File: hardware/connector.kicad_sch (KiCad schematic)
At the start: 5 parts, among them J1 SAFETY_SUPPLY, J2 SWDIO_CONN, J3 SENSORS, J4 VALVES, J5 MAIN

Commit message: DRC fixes part 1
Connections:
- net +24V renamed 24v input
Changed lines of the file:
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@@
-    (stroke (width 0) (type default) (color 0 0 0 0))
-  )
-  (wire (pts (xy 78.74 118.11) (xy 78.74 120.65))
     (stroke (width 0) (type default) (color 0 0 0 0))
   )
@@
     )
   )
+  (global_label "24v input" (shape input) (at 78.74 120.65 180) (fields_autoplaced)
+    (effects (font (size 1.27 1.27)) (justify right))
+    (property "Intersheet References" "${INTERSHEET_REFS}" (id 0) (at 67.195 120.5706 0)
+      (effects (font (size 1.27 1.27)) (justify right) hide)
+    )
+  )
   (global_label "NRST" (shape input) (at 201.93 87.63 180) (fields_autoplaced)
     (effects (font (size 1.27 1.27) italic) (justify right))
@@
       (effects (font (size 1.27 1.27)) hide)
     )
-    (pin "1")
-  )
-  (symbol (lib_id "power:+24V") (at 78.74 118.11 0) (unit 1)
-    (in_bom yes) (on_board yes) (fields_autoplaced)
-    (property "Reference" "#PWR0108" (id 0) (at 78.74 121.92 0)
-      (effects (font (size 1.27 1.27)) hide)
-    )
-    (property "Value" "+24V" (id 1) (at 78.74 113.03 0))
-    (property "Footprint" "" (id 2) (at 78.74 118.11 0)
-      (effects (font (size 1.27 1.27)) hide)
-    )
-    (property "Datasheet" "" (id 3) (at 78.74 118.11 0)
-      (effects (font (size 1.27 1.27)) hide)
-    )

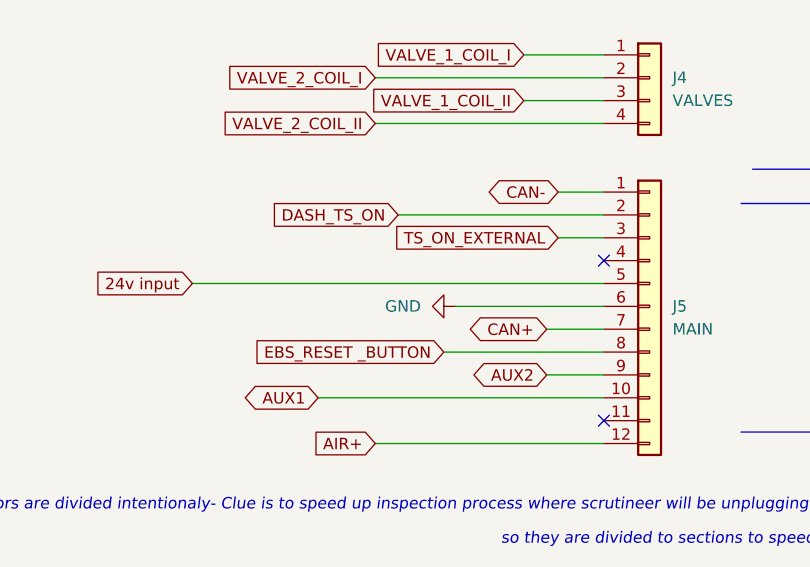
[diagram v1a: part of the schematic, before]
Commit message: Alpha 1.0 Hardware relase. 0xDRC state, improved aesthetics and signal integrity
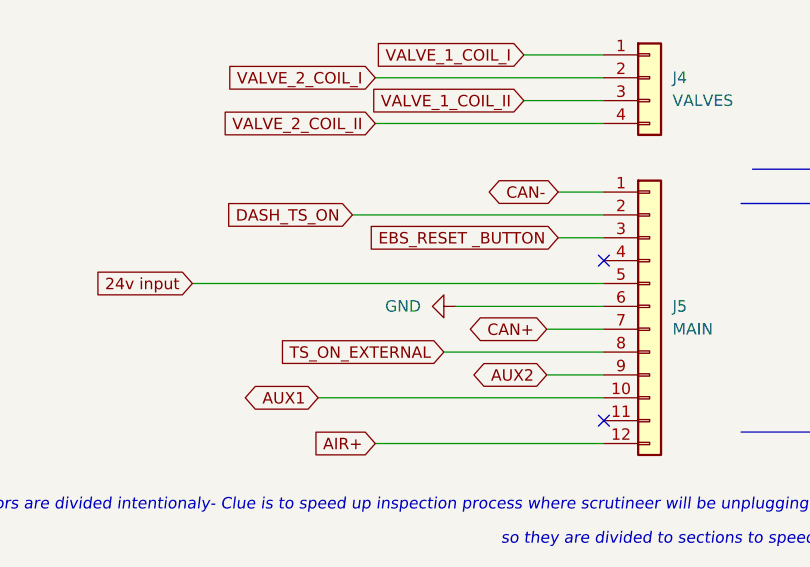
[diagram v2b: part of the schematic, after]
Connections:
- net EBS_RESET _BUTTON: now also J5.3 (Pin_3); no longer J5.8 (Pin_8)
- net TS_ON_EXTERNAL: now also J5.8 (Pin_8); no longer J5.3 (Pin_3)
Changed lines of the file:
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@@
     (stroke (width 0) (type default) (color 0 0 0 0))
   )
-  (wire (pts (xy 124.46 113.03) (xy 101.6 113.03))
+  (wire (pts (xy 124.46 113.03) (xy 96.52 113.03))
     (stroke (width 0) (type default) (color 0 0 0 0))
   )
@@
     )
   )
+  (global_label "TS_ON_EXTERNAL" (shape input) (at 106.68 128.27 180) (fields_autoplaced)
+    (effects (font (size 1.27 1.27)) (justify right))
+    (property "Intersheet References" "${INTERSHEET_REFS}" (id 0) (at 88.3012 128.3494 0)
+      (effects (font (size 1.27 1.27)) (justify right) hide)
+    )
+  )
   (global_label "VALVE_2_COIL_I" (shape input) (at 99.06 97.79 180) (fields_autoplaced)
     (effects (font (size 1.27 1.27)) (justify right))
@@
     (effects (font (size 1.27 1.27)) (justify right))
     (property "Intersheet References" "${INTERSHEET_REFS}" (id 0) (at 98.7636 95.1706 0)
+      (effects (font (size 1.27 1.27)) (justify right) hide)
+    )
+  )
+  (global_label "EBS_RESET _BUTTON" (shape input) (at 119.38 115.57 180) (fields_autoplaced)
+    (effects (font (size 1.27 1.27)) (justify right))
+    (property "Intersheet References" "${INTERSHEET_REFS}" (id 0) (at 97.4936 115.6494 0)
       (effects (font (size 1.27 1.27)) (justify right) hide)
     )
@@
     )
   )
-  (global_label "DASH_TS_ON" (shape input) (at 101.6 113.03 180) (fields_autoplaced)
+  (global_label "DASH_TS_ON" (shape input) (at 96.52 113.03 180) (fields_autoplaced)
     (effects (font (size 1.27 1.27)) (justify right))
-    (property "Intersheet References" "${INTERSHEET_REFS}" (id 0) (at 87.515 113.1094 0)
+    (property "Intersheet References" "${INTERSHEET_REFS}" (id 0) (at 82.435 113.1094 0)
       (effects (font (size 1.27 1.27)) (justify right) hide)
     )
@@
       (effects (font (size 1.27 1.27)) (justify right) hide)
     )
-  )
-  (global_label "EBS_RESET _BUTTON" (shape input) (at 106.68 128.27 180) (fields_autoplaced)
-    (effects (font (size 1.27 1.27)) (justify right))
-    (property "Intersheet References" "${INTERSHEET_REFS}" (id 0) (at 84.7936 128.3494 0)
-      (effects (font (size 1.27 1.27)) (justify right) hide)
-    )
-  )
-  (global_label "TS_ON_EXTERNAL" (shape input) (at 119.38 115.57 180) (fields_autoplaced)
-    (effects (font (size 1.27 1.27)) (justify right))
-    (property "Intersheet References" "${INTERSHEET_REFS}" (id 0) (at 101.0012 115.6494 0)
-      (effects (font (size 1.27 1.27)) (justify right) hide)
-    )

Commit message: minor aestethics improvement
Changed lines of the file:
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@@
   (no_connect (at 124.46 87.63))
   (no_connect (at 124.46 72.39))
-  (wire (pts (xy 99.06 138.43) (xy 124.46 138.43))
+  (wire (pts (xy 118.11 138.43) (xy 124.46 138.43))
     (stroke (width 0) (type default) (color 0 0 0 0))
   )
@@
     (stroke (width 0) (type default) (color 0 0 0 0))
   )
-  (wire (pts (xy 99.06 102.87) (xy 124.46 102.87))
+  (wire (pts (xy 97.79 102.87) (xy 124.46 102.87))
     (stroke (width 0) (type default) (color 0 0 0 0))
   )
@@
     (stroke (width 0) (type default) (color 0 0 0 0))
   )
-  (wire (pts (xy 78.74 120.65) (xy 124.46 120.65))
+  (wire (pts (xy 97.79 120.65) (xy 124.46 120.65))
     (stroke (width 0) (type default) (color 0 0 0 0))
   )
@@
     (stroke (width 0) (type default) (color 0 0 0 0))
   )
-  (wire (pts (xy 124.46 133.35) (xy 92.71 133.35))
+  (wire (pts (xy 124.46 133.35) (xy 107.95 133.35))
     (stroke (width 0) (type default) (color 0 0 0 0))
   )
@@
     (stroke (width 0) (type default) (color 0 0 0 0))
   )
-  (wire (pts (xy 99.06 97.79) (xy 124.46 97.79))
+  (wire (pts (xy 97.79 97.79) (xy 124.46 97.79))
     (stroke (width 0) (type default) (color 0 0 0 0))
   )
@@
     )
   )
-  (global_label "AIR+" (shape input) (at 99.06 138.43 180) (fields_autoplaced)
-    (effects (font (size 1.27 1.27)) (justify right))
-    (property "Intersheet References" "${INTERSHEET_REFS}" (id 0) (at 92.1112 138.5094 0)
+  (global_label "AIR+" (shape input) (at 118.11 138.43 180) (fields_autoplaced)
+    (effects (font (size 1.27 1.27)) (justify right))
+    (property "Intersheet References" "${INTERSHEET_REFS}" (id 0) (at 111.1612 138.5094 0)
       (effects (font (size 1.27 1.27)) (justify right) hide)
     )
@@
     )
   )
-  (global_label "VALVE_2_COIL_I" (shape input) (at 99.06 97.79 180) (fields_autoplaced)
-    (effects (font (size 1.27 1.27)) (justify right))
-    (property "Intersheet References" "${INTERSHEET_REFS}" (id 0) (at 82.2536 97.7106 0)
+  (global_label "VALVE_2_COIL_I" (shape input) (at 97.79 97.79 180) (fields_autoplaced)
+    (effects (font (size 1.27 1.27)) (justify right))
+    (property "Intersheet References" "${INTERSHEET_REFS}" (id 0) (at 80.9836 97.7106 0)
       (effects (font (size 1.27 1.27)) (justify right) hide)
     )
@@
     )
   )
-  (global_label "VALVE_2_COIL_II" (shape input) (at 99.06 102.87 180) (fields_autoplaced)
-    (effects (font (size 1.27 1.27)) (justify right))
-    (property "Intersheet References" "${INTERSHEET_REFS}" (id 0) (at 81.6488 102.7906 0)
+  (global_label "VALVE_2_COIL_II" (shape input) (at 97.79 102.87 180) (fields_autoplaced)
+    (effects (font (size 1.27 1.27)) (justify right))
+    (property "Intersheet References" "${INTERSHEET_REFS}" (id 0) (at 80.3788 102.7906 0)
       (effects (font (size 1.27 1.27)) (justify right) hide)
     )
@@
     )
   )
-  (global_label "AUX1" (shape bidirectional) (at 92.71 133.35 180) (fields_autoplaced)
-    (effects (font (size 1.27 1.27)) (justify right))
-    (property "Intersheet References" "${INTERSHEET_REFS}" (id 0) (at 85.4588 133.2706 0)
+  (global_label "AUX1" (shape bidirectional) (at 107.95 133.35 180) (fields_autoplaced)
+    (effects (font (size 1.27 1.27)) (justify right))
+    (property "Intersheet References" "${INTERSHEET_REFS}" (id 0) (at 100.6988 133.2706 0)
       (effects (font (size 1.27 1.27)) (justify right) hide)
     )
@@
     )
   )
-  (global_label "24v input" (shape input) (at 78.74 120.65 180) (fields_autoplaced)
-    (effects (font (size 1.27 1.27)) (justify right))
-    (property "Intersheet References" "${INTERSHEET_REFS}" (id 0) (at 67.195 120.5706 0)
-      (effects (font (size 1.27 1.27)) (justify right) hide)
-    )
+  (global_label "24v input" (shape input) (at 97.79 120.65 180) (fields_autoplaced)
+    (effects (font (size 1.27 1.27)) (justify right))
+    (property "Intersheet References" "${INTERSHEET_REFS}" (id 0) (at 86.245 120.5706 0)
+      (effects (font (size 1.27 1.27)) (justify right) hide)
+    )

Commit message: GND improvement after Review (taka masa ze sie wengoz zesra)
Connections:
- net LINE: now also J1.3 (Pin_3); no longer J1.1 (Pin_1)
- net SAFETY_OUT: now also J1.4 (Pin_4); no longer J1.3 (Pin_3)
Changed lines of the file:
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@@
   )
   (no_connect (at 124.46 118.11))
+  (no_connect (at 124.46 64.77))
   (no_connect (at 124.46 135.89))
   (no_connect (at 124.46 87.63))
-  (no_connect (at 124.46 72.39))
   (wire (pts (xy 118.11 138.43) (xy 124.46 138.43))
     (stroke (width 0) (type default) (color 0 0 0 0))
   )
+  (wire (pts (xy 99.06 69.85) (xy 124.46 69.85))
+    (stroke (width 0) (type default) (color 0 0 0 0))
+  )
   (wire (pts (xy 119.38 110.49) (xy 124.46 110.49))
     (stroke (width 0) (type default) (color 0 0 0 0))
@@
     (stroke (width 0) (type default) (color 0 0 0 0))
   )
-  (wire (pts (xy 106.68 69.85) (xy 124.46 69.85))
-    (stroke (width 0) (type default) (color 0 0 0 0))
-  )
   (wire (pts (xy 212.09 85.09) (xy 218.44 85.09))
     (stroke (width 0) (type default) (color 0 0 0 0))
@@
     (stroke (width 0) (type default) (color 0 0 0 0))
   )
-  (wire (pts (xy 123.19 67.31) (xy 124.46 67.31))
+  (wire (pts (xy 121.92 67.31) (xy 124.46 67.31))
     (stroke (width 0) (type default) (color 0 0 0 0))
   )
@@
     (stroke (width 0) (type default) (color 0 0 0 0))
   )
+  (wire (pts (xy 121.92 72.39) (xy 124.46 72.39))
+    (stroke (width 0) (type default) (color 0 0 0 0))
+  )
   (wire (pts (xy 116.84 85.09) (xy 124.46 85.09))
     (stroke (width 0) (type default) (color 0 0 0 0))
@@
   (wire (pts (xy 124.46 113.03) (xy 96.52 113.03))
     (stroke (width 0) (type default) (color 0 0 0 0))
-  )
-  (wire (pts (xy 111.76 64.77) (xy 124.46 64.77))
-    (stroke (width 0) (type default) (color 0 0 0 0))
-  )
-  (text "(AFTER RES 2)" (at 113.03 64.77 0)
-    (effects (font (size 0.7 0.7)) (justify left bottom))
   )
   (text "10pin version not in stock ;/" (at 160.02 129.54 0)
@@
   (text "\nM80-5L11242MC\n" (at 161.29 125.73 0)
     (effects (font (size 1.27 1.27)) (justify left bottom))
+  )
+  (text "(AFTER RES 2)" (at 99.06 68.58 0)
+    (effects (font (size 0.7 0.7)) (justify left bottom))
   )
   (text "M80-5L10442MC" (at 157.48 88.9 0)
@@
     )
   )
-  (global_label "SAFETY_OUT" (shape output) (at 106.68 69.85 180) (fields_autoplaced)
-    (effects (font (size 1.27 1.27)) (justify right))
-    (property "Intersheet References" "${INTERSHEET_REFS}" (id 0) (at 93.0788 69.7706 0)
-      (effects (font (size 1.27 1.27)) (justify right) hide)
-    )
-  )
   (global_label "SWDCLK" (shape input) (at 213.36 80.01 180) (fields_autoplaced)
     (effects (font (size 1.27 1.27) italic) (justify right))
@@
     )
   )
-  (global_label "SAFETY_IN" (shape input) (at 123.19 67.31 180) (fields_autoplaced)
-    (effects (font (size 1.27 1.27)) (justify right))
-    (property "Intersheet References" "${INTERSHEET_REFS}" (id 0) (at 111.2821 67.2306 0)
+  (global_label "SAFETY_IN" (shape input) (at 121.92 67.31 180) (fields_autoplaced)
+    (effects (font (size 1.27 1.27)) (justify right))
+    (property "Intersheet References" "${INTERSHEET_REFS}" (id 0) (at 110.0121 67.2306 0)
+      (effects (font (size 1.27 1.27)) (justify right) hide)
+    )
+  )
+  (global_label "SAFETY_OUT" (shape output) (at 121.92 72.39 180) (fields_autoplaced)
+    (effects (font (size 1.27 1.27)) (justify right))
+    (property "Intersheet References" "${INTERSHEET_REFS}" (id 0) (at 108.3188 72.3106 0)
       (effects (font (size 1.27 1.27)) (justify right) hide)
     )
@@
     (pin "3")
     (pin "4")
-  )
-  (symbol (lib_id "power:LINE") (at 111.76 64.77 90) (unit 1)
-    (in_bom yes) (on_board yes)
-    (property "Reference" "#PWR047" (id 0) (at 115.57 64.77 0)
-      (effects (font (size 1.27 1.27)) hide)
-    )
-    (property "Value" "LINE" (id 1) (at 104.14 64.77 90)
-      (effects (font (size 1.27 1.27)) (justify right))
-    )
-    (property "Footprint" "" (id 2) (at 111.76 64.77 0)
-      (effects (font (size 1.27 1.27)) hide)
-    )
-    (property "Datasheet" "" (id 3) (at 111.76 64.77 0)
-      (effects (font (size 1.27 1.27)) hide)
-    )
-    (pin "1")
   )
   (symbol (lib_id "power:+3V3") (at 214.63 74.93 0) (unit 1)
@@
       (effects (font (size 1.27 1.27)) hide)
     )
+    (pin "1")
+  )
+  (symbol (lib_id "power:LINE") (at 99.06 69.85 90) (unit 1)
+    (in_bom yes) (on_board yes)
+    (property "Reference" "#PWR0106" (id 0) (at 102.87 69.85 0)
+      (effects (font (size 1.27 1.27)) hide)
+    )
+    (property "Value" "LINE" (id 1) (at 91.44 69.85 90)
+      (effects (font (size 1.27 1.27)) (justify right))
+    )
+    (property "Footprint" "" (id 2) (at 99.06 69.85 0)
+      (effects (font (size 1.27 1.27)) hide)
+    )
+    (property "Datasheet" "" (id 3) (at 99.06 69.85 0)
+      (effects (font (size 1.27 1.27)) hide)
+    )
